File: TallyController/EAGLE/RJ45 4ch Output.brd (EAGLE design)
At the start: 86 x 26.7 mm, 10 parts, among them J1 RJHSE-5381-04

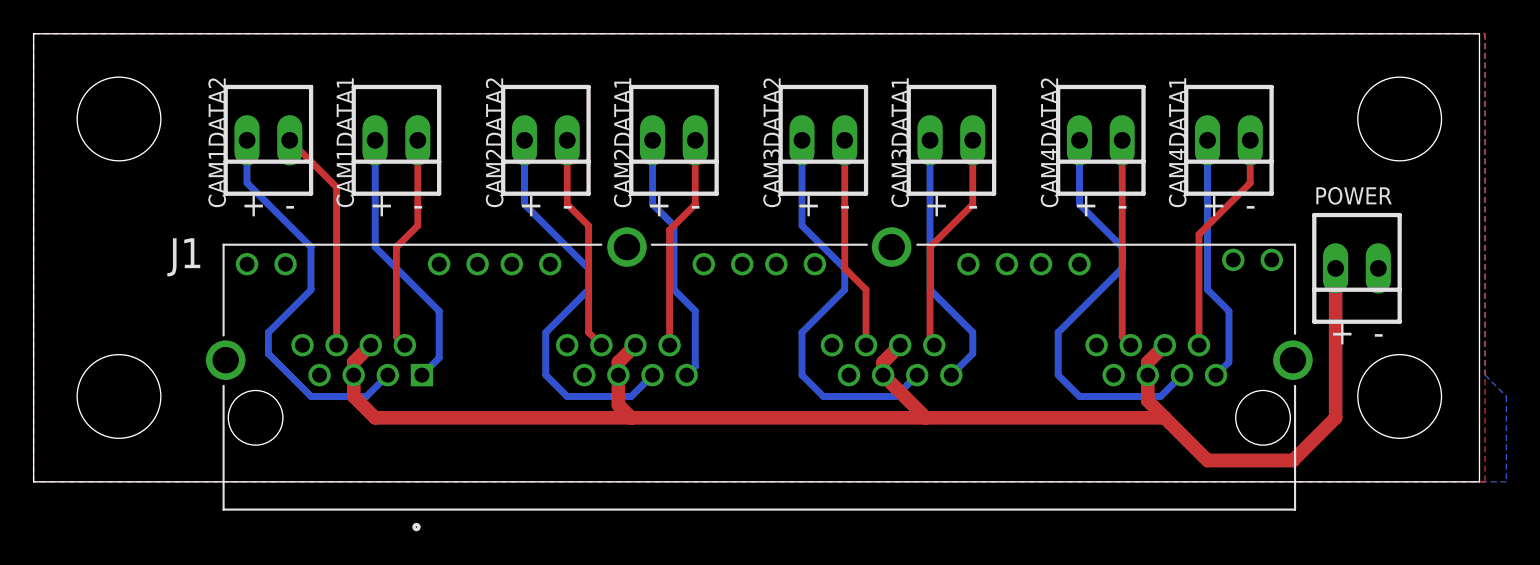
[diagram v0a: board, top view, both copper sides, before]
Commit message: Slim down some spacings to possibly use some 8 pin headers instead of 4x 2pin.  Fix hole drill sizes.
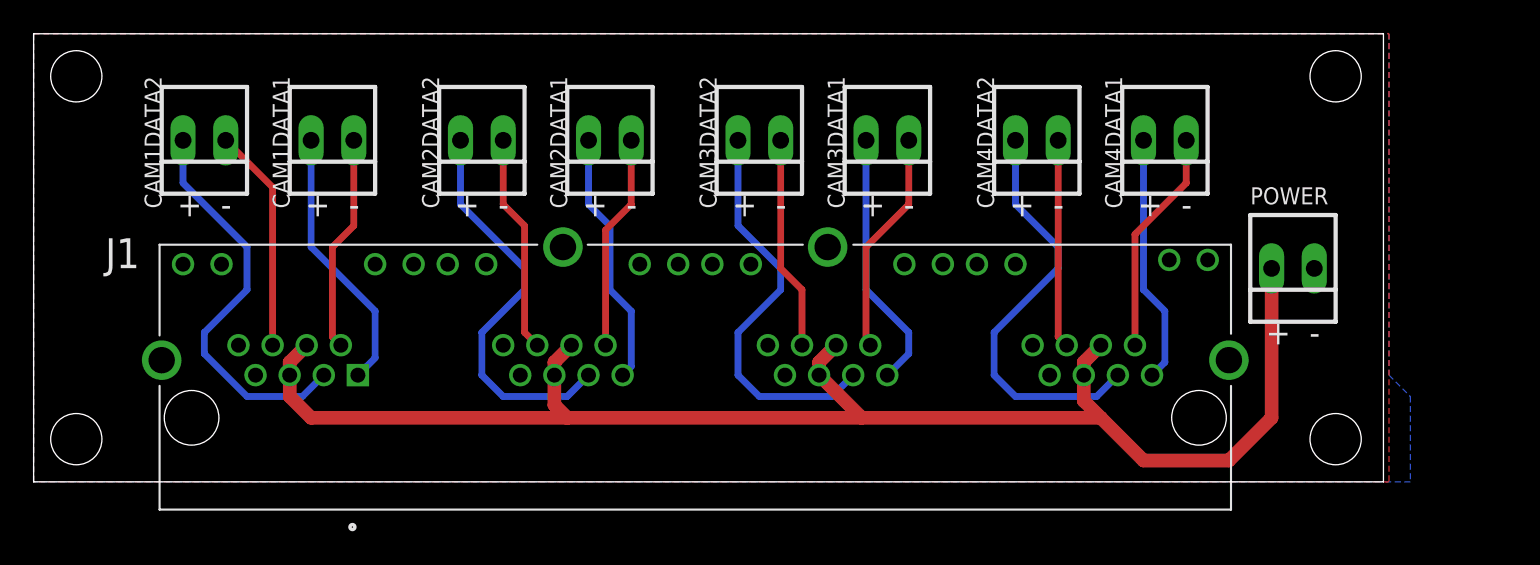
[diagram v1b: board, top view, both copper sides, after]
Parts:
- moved CAM2DATA1 3.81 mm to (34.3, 20.3)
- moved CAM3DATA1 3.81 mm to (50.8, 20.3)
- moved CAM3DATA2 3.81 mm to (43.2, 20.3)
- moved CAM4DATA1 3.81 mm to (67.3, 20.3)
- moved CAM4DATA2 3.81 mm to (59.7, 20.3)
- moved J1 3.81 mm to (39.4, 3.81)
- moved CAM1DATA2 3.81 mm to (10.2, 20.3)
- moved CAM1DATA1 3.81 mm to (17.8, 20.3)
- moved CAM2DATA2 3.81 mm to (26.7, 20.3)
- moved POWER 3.81 mm to (74.9, 12.7)
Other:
- board size 86 x 26.7 mm -> 80.3 x 26.7 mm

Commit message: Go through and fix notation on RS485 wiring everywhere to use the standard A/B notation.
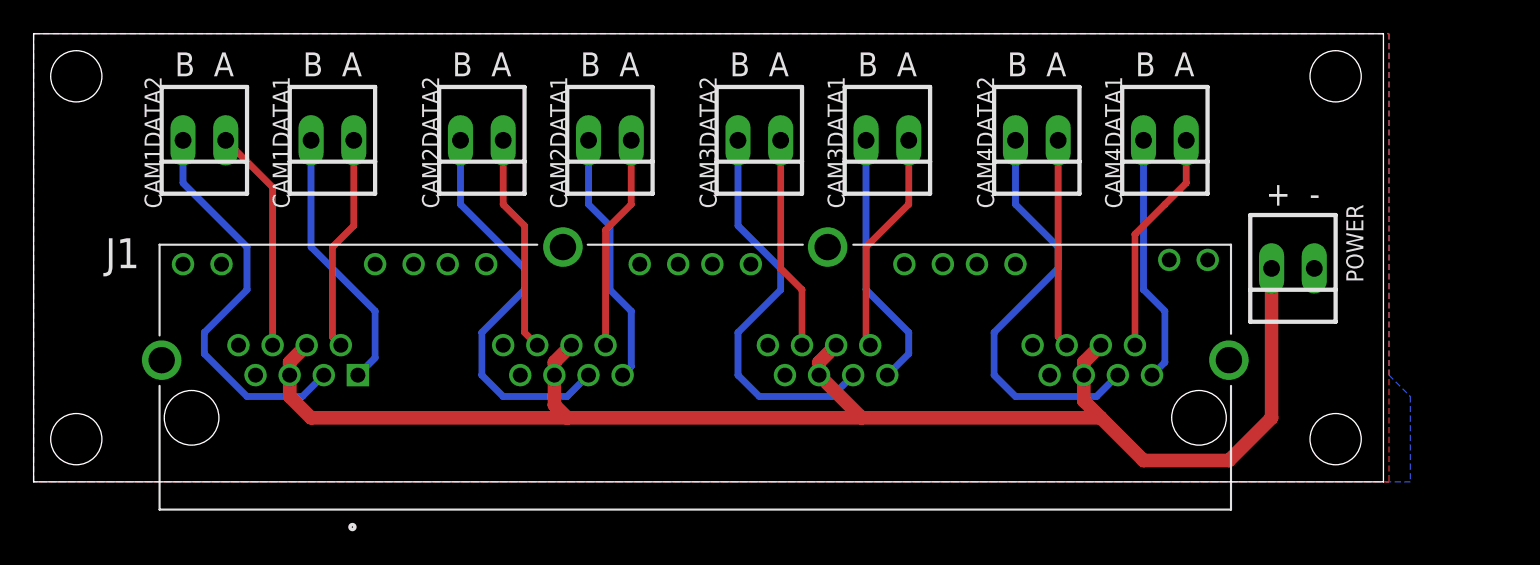
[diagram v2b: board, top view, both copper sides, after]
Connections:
- net C1DATA1+ renamed C1DATA1B
- net C1DATA1- renamed C1DATA1A
- net C1DATA2+ renamed C1DATA2B
- net C1DATA2- renamed C1DATA2A
- net C2DATA1+ renamed C2DATA1B
- net C2DATA1- renamed C2DATA1A
- net C2DATA2+ renamed C2DATA2B
- net C2DATA2- renamed C2DATA2A
- net C3DATA1+ renamed C3DATA1B
- net C3DATA1- renamed C3DATA1A
- net C3DATA2+ renamed C3DATA2B
- net C3DATA2- renamed C3DATA2A
- net C4DATA1+ renamed C4DATA1B
- net C4DATA1- renamed C4DATA1A
- net C4DATA2+ renamed C4DATA2B
- net C4DATA2- renamed C4DATA2A
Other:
- board text added: "B A"
